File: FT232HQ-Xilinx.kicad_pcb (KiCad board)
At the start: 2 copper layers, 30.5 x 20.3 mm, 37 parts, among them J1 USB_C_Receptacle_USB2.0_16P, J2 Conn_01x03_MountingPin, J3 Conn_02x05_Odd_Even, U1 TLV9061xDBV, U3 SN74AVC4T774PW, U4 12M, U5 FT232H, U6 93LCxxBxxOT

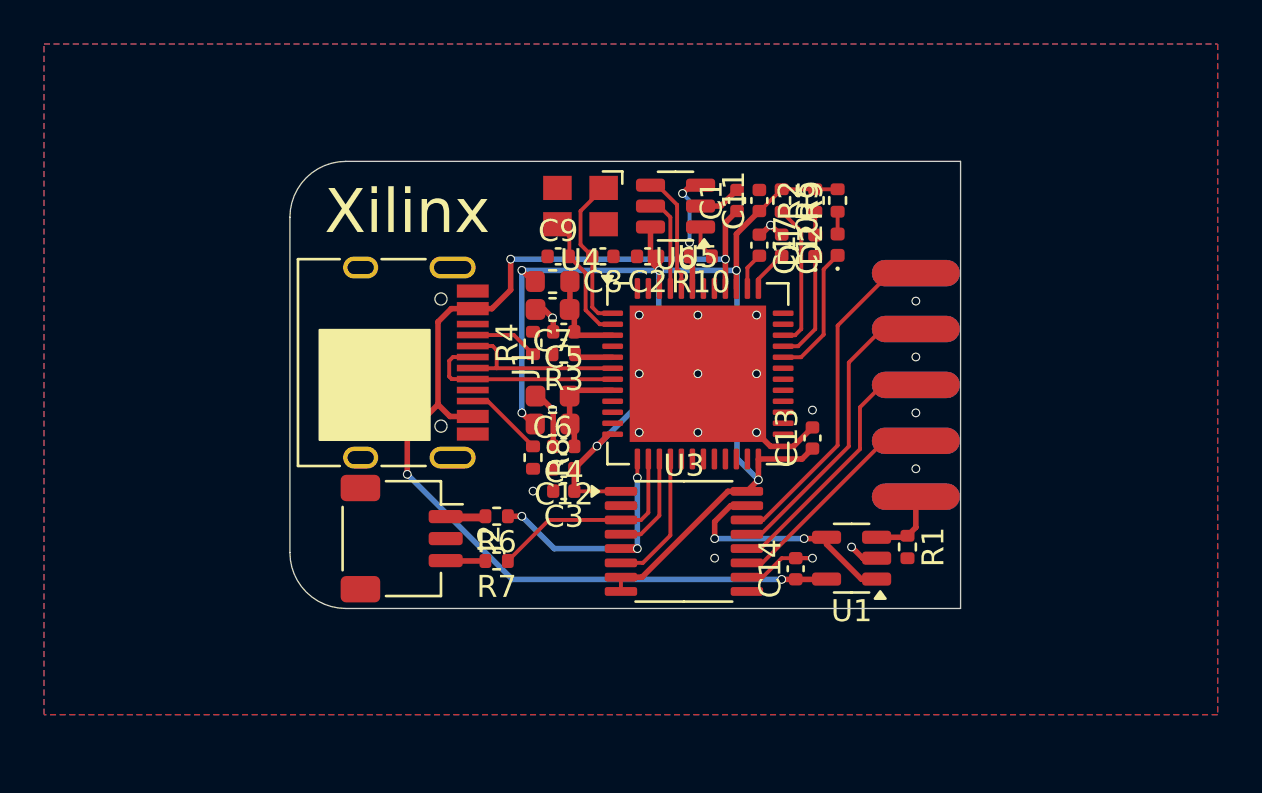
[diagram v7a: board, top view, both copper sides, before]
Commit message: add text
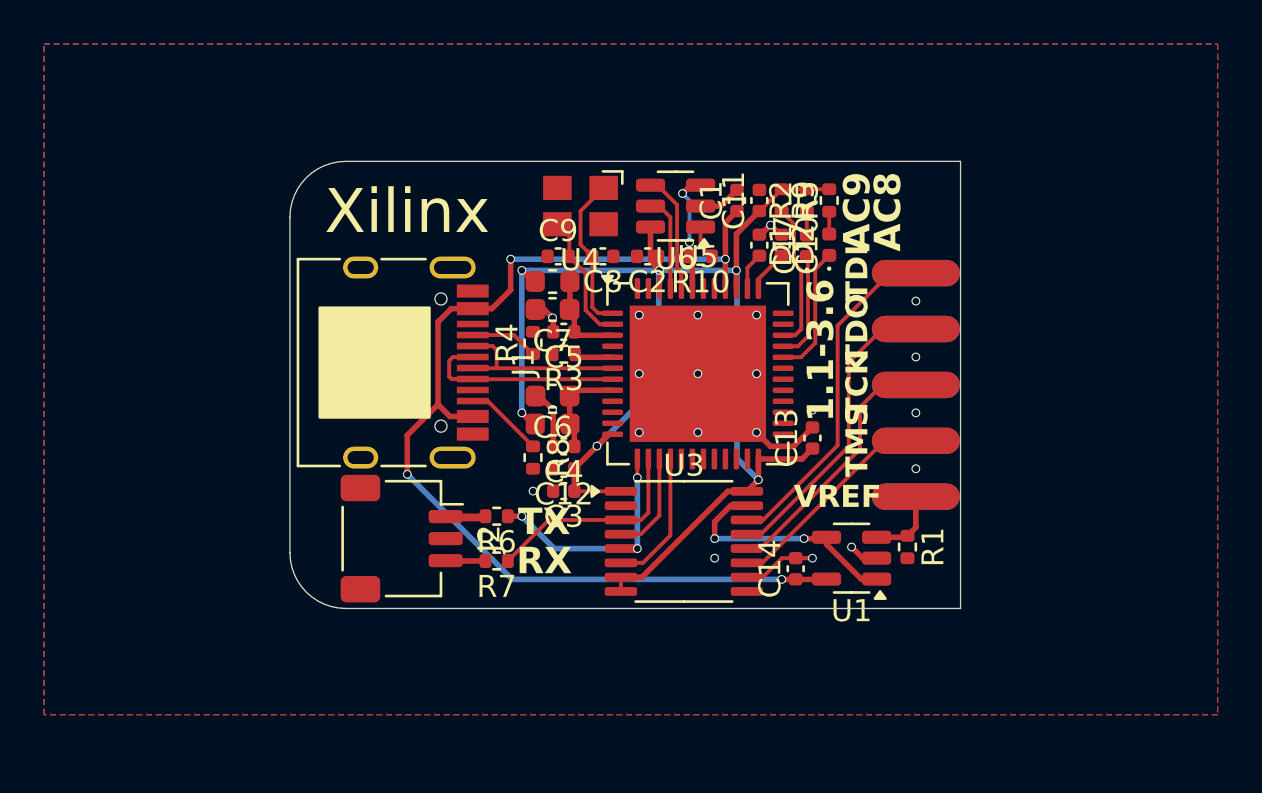
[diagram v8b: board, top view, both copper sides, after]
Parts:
- moved D1 0.38 mm to (147.3, 69.7)
- moved D2 0.38 mm to (148.3, 69.6)
- moved R2 0.38 mm to (147.3, 67.6)
- moved R9 0.38 mm to (148.3, 67.6)
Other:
- board text added: "1.1-3.6"
- board text added: "AC8"
- board text added: "AC9"
- board text added: "RX"
- board text added: "TX"
- board text removed: "1.1V-3.6V"
- board text removed: "GND"
- board text removed: "NC"
